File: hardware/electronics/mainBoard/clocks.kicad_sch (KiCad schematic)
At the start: 6 parts, among them X1 ECS-327ATQ2016MV, X2 ECS-2016MVQ, X3 ECS-2016MVQ

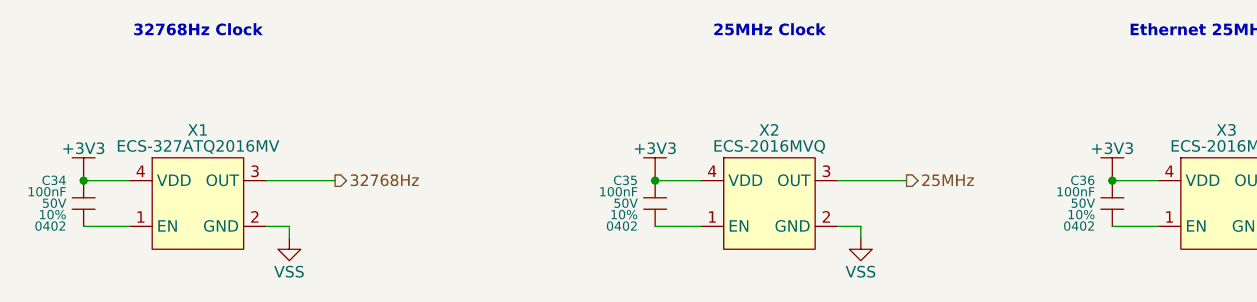
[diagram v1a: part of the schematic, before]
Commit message: updated symbol refs
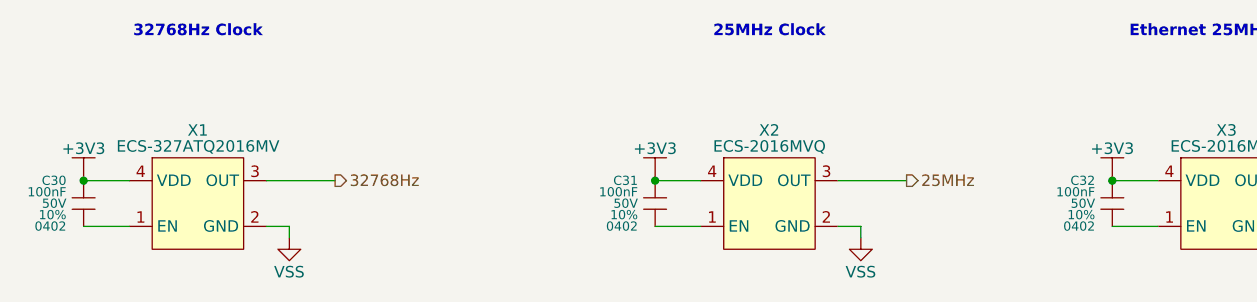
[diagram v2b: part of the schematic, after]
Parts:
- renumbered C34 to C30, C35 to C31, C36 to C32
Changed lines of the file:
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@@
 		(dnp no)
 		(fields_autoplaced yes)
-		(property "Reference" "#PWR082"
+		(property "Reference" "#PWR077"
 			(at 177.8 105.41 0)
 			(effects
@@
 			(project "mainBoard"
 				(path "/be16e32f-2ccf-4272-9ec7-94d5fe7a55e0/7c38f482-70e6-459c-b3af-acf1cdcfd3ea"
-					(reference "#PWR082")
+					(reference "#PWR077")
 					(unit 1)
 				)
@@
 		(dnp no)
 		(fields_autoplaced yes)
-		(property "Reference" "#PWR083"
+		(property "Reference" "#PWR080"
 			(at 200.66 111.76 0)
 			(effects
@@
 			(project "mainBoard"
 				(path "/be16e32f-2ccf-4272-9ec7-94d5fe7a55e0/7c38f482-70e6-459c-b3af-acf1cdcfd3ea"
-					(reference "#PWR083")
+					(reference "#PWR080")
 					(unit 1)
 				)
@@
 		(on_board yes)
 		(dnp no)
-		(property "Reference" "C35"
+		(property "Reference" "C31"
 			(at 125.095 105.41 0)
 			(do_not_autoplace yes)
@@
 			(project "mainBoard"
 				(path "/be16e32f-2ccf-4272-9ec7-94d5fe7a55e0/7c38f482-70e6-459c-b3af-acf1cdcfd3ea"
-					(reference "C35")
+					(reference "C31")
 					(unit 1)
 				)
@@
 		(on_board yes)
 		(dnp no)
-		(property "Reference" "C34"
+		(property "Reference" "C30"
 			(at 61.595 105.41 0)
 			(do_not_autoplace yes)
@@
 			(project "mainBoard"
 				(path "/be16e32f-2ccf-4272-9ec7-94d5fe7a55e0/7c38f482-70e6-459c-b3af-acf1cdcfd3ea"
-					(reference "C34")
+					(reference "C30")
 					(unit 1)
 				)
@@
 		(dnp no)
 		(fields_autoplaced yes)
-		(property "Reference" "#PWR081"
+		(property "Reference" "#PWR079"
 			(at 149.86 111.76 0)
 			(effects
@@
 			(project "mainBoard"
 				(path "/be16e32f-2ccf-4272-9ec7-94d5fe7a55e0/7c38f482-70e6-459c-b3af-acf1cdcfd3ea"
-					(reference "#PWR081")
+					(reference "#PWR079")
 					(unit 1)
 				)
@@
 		(dnp no)
 		(fields_autoplaced yes)
-		(property "Reference" "#PWR078"
+		(property "Reference" "#PWR075"
 			(at 63.5 105.41 0)
 			(effects
@@
 			(project "mainBoard"
 				(path "/be16e32f-2ccf-4272-9ec7-94d5fe7a55e0/7c38f482-70e6-459c-b3af-acf1cdcfd3ea"
-					(reference "#PWR078")
+					(reference "#PWR075")
 					(unit 1)
 				)
@@
 		(on_board yes)
 		(dnp no)
-		(property "Reference" "C36"
+		(property "Reference" "C32"
 			(at 175.895 105.41 0)
 			(do_not_autoplace yes)
@@
 			(project "mainBoard"
 				(path "/be16e32f-2ccf-4272-9ec7-94d5fe7a55e0/7c38f482-70e6-459c-b3af-acf1cdcfd3ea"
-					(reference "C36")
+					(reference "C32")
 					(unit 1)
 				)
@@
 		(dnp no)
 		(fields_autoplaced yes)
-		(property "Reference" "#PWR079"
+		(property "Reference" "#PWR078"
 			(at 86.36 111.76 0)
 			(effects
@@
 			(project "mainBoard"
 				(path "/be16e32f-2ccf-4272-9ec7-94d5fe7a55e0/7c38f482-70e6-459c-b3af-acf1cdcfd3ea"
-					(reference "#PWR079")
+					(reference "#PWR078")
 					(unit 1)
 				)
@@
 		(dnp no)
 		(fields_autoplaced yes)
-		(property "Reference" "#PWR080"
+		(property "Reference" "#PWR076"
 			(at 127 105.41 0)
 			(effects
@@
 			(project "mainBoard"
 				(path "/be16e32f-2ccf-4272-9ec7-94d5fe7a55e0/7c38f482-70e6-459c-b3af-acf1cdcfd3ea"
-					(reference "#PWR080")
-					(unit 1)
-				)
+					(reference "#PWR076")
+					(unit 1)
+				)

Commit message: assigned FPs
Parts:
- X1: footprint (none) -> lib_crystals:ECS-xxxATQ2016MV
- X2, X3: footprint (none) -> lib_crystals:ECS-2016MV
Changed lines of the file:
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@@
 			)
 		)
-		(property "Footprint" ""
+		(property "Footprint" "lib_crystals:ECS-xxxATQ2016MV"
 			(at 76.2 107.95 0)
 			(effects
@@
 			)
 		)
-		(property "Footprint" ""
+		(property "Footprint" "lib_crystals:ECS-2016MV"
 			(at 139.7 107.95 0)
 			(effects
@@
 			)
 		)
-		(property "Footprint" ""
+		(property "Footprint" "lib_crystals:ECS-2016MV"
 			(at 190.5 107.95 0)
 			(effects

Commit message: assigned footprints
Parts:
- C30, C31, C32: footprint (none) -> lib_passives:GCM0402
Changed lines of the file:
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@@
 	(title_block
 		(title "Clocks")
-		(date "2025-03-15")
+		(date "2025-03-20")
 		(rev "1")
 		(comment 2 "PROTOTYPE")
@@
 		(dnp no)
 		(fields_autoplaced yes)
-		(property "Reference" "#PWR077"
+		(property "Reference" "#PWR079"
 			(at 177.8 105.41 0)
 			(effects
@@
 			(project "mainBoard"
 				(path "/be16e32f-2ccf-4272-9ec7-94d5fe7a55e0/7c38f482-70e6-459c-b3af-acf1cdcfd3ea"
-					(reference "#PWR077")
+					(reference "#PWR079")
 					(unit 1)
 				)
@@
 			)
 		)
-		(property "Footprint" ""
+		(property "Footprint" "lib_passives:GCM0402"
 			(at 127 106.045 0)
 			(effects
@@
 			)
 		)
-		(property "Footprint" ""
+		(property "Footprint" "lib_passives:GCM0402"
 			(at 63.5 106.045 0)
 			(effects
@@
 		(dnp no)
 		(fields_autoplaced yes)
-		(property "Reference" "#PWR079"
+		(property "Reference" "#PWR078"
 			(at 149.86 111.76 0)
 			(effects
@@
 			(project "mainBoard"
 				(path "/be16e32f-2ccf-4272-9ec7-94d5fe7a55e0/7c38f482-70e6-459c-b3af-acf1cdcfd3ea"
-					(reference "#PWR079")
+					(reference "#PWR078")
 					(unit 1)
 				)
@@
 			)
 		)
-		(property "Footprint" ""
+		(property "Footprint" "lib_passives:GCM0402"
 			(at 177.8 106.045 0)
 			(effects
@@
 		(dnp no)
 		(fields_autoplaced yes)
-		(property "Reference" "#PWR078"
+		(property "Reference" "#PWR076"
 			(at 86.36 111.76 0)
 			(effects
@@
 			(project "mainBoard"
 				(path "/be16e32f-2ccf-4272-9ec7-94d5fe7a55e0/7c38f482-70e6-459c-b3af-acf1cdcfd3ea"
-					(reference "#PWR078")
+					(reference "#PWR076")
 					(unit 1)
 				)
@@
 		(dnp no)
 		(fields_autoplaced yes)
-		(property "Reference" "#PWR076"
+		(property "Reference" "#PWR077"
 			(at 127 105.41 0)
 			(effects
@@
 			(project "mainBoard"
 				(path "/be16e32f-2ccf-4272-9ec7-94d5fe7a55e0/7c38f482-70e6-459c-b3af-acf1cdcfd3ea"
-					(reference "#PWR076")
+					(reference "#PWR077")
 					(unit 1)
 				)

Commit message: added debugger stuff
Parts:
- added C154, C155: 100nF, lib_passives:GCM0402, symbol lib_sch:C
- added X4: ECS-327ATQ2016MV, lib_crystals:ECS-xxxATQ2016MV, symbol lib_sch:ECS_XTAL_4-SMD
- added X5: ECS-2016MVQ-120, lib_crystals:ECS-2016MV, symbol lib_sch:ECS_XTAL_4-SMD
- X2: value ECS-2016MVQ -> ECS-2016MVQ-250
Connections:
- net VSS: now also X4.2 (GND), X5.2 (GND)
- new net: C155.2, X5.1 (EN)
- new net: C154.2, X4.1 (EN)
- new net +3V3_DBG_H7: C154.1, C155.1, X4.4 (VDD), X5.4 (VDD)
- new net Debug_12MHz: X5.3 (OUT)
- new net Debug_32768Hz: X4.3 (OUT)
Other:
- note added: "12MHz Debugger Clock"
- note added: "32.768kHz Clock"
- note added: "32.768kHz Debugger Clock"
- note removed: "32768Hz Clock"
- moved on the sheet: C30, C31, C32, X1, X2, X3

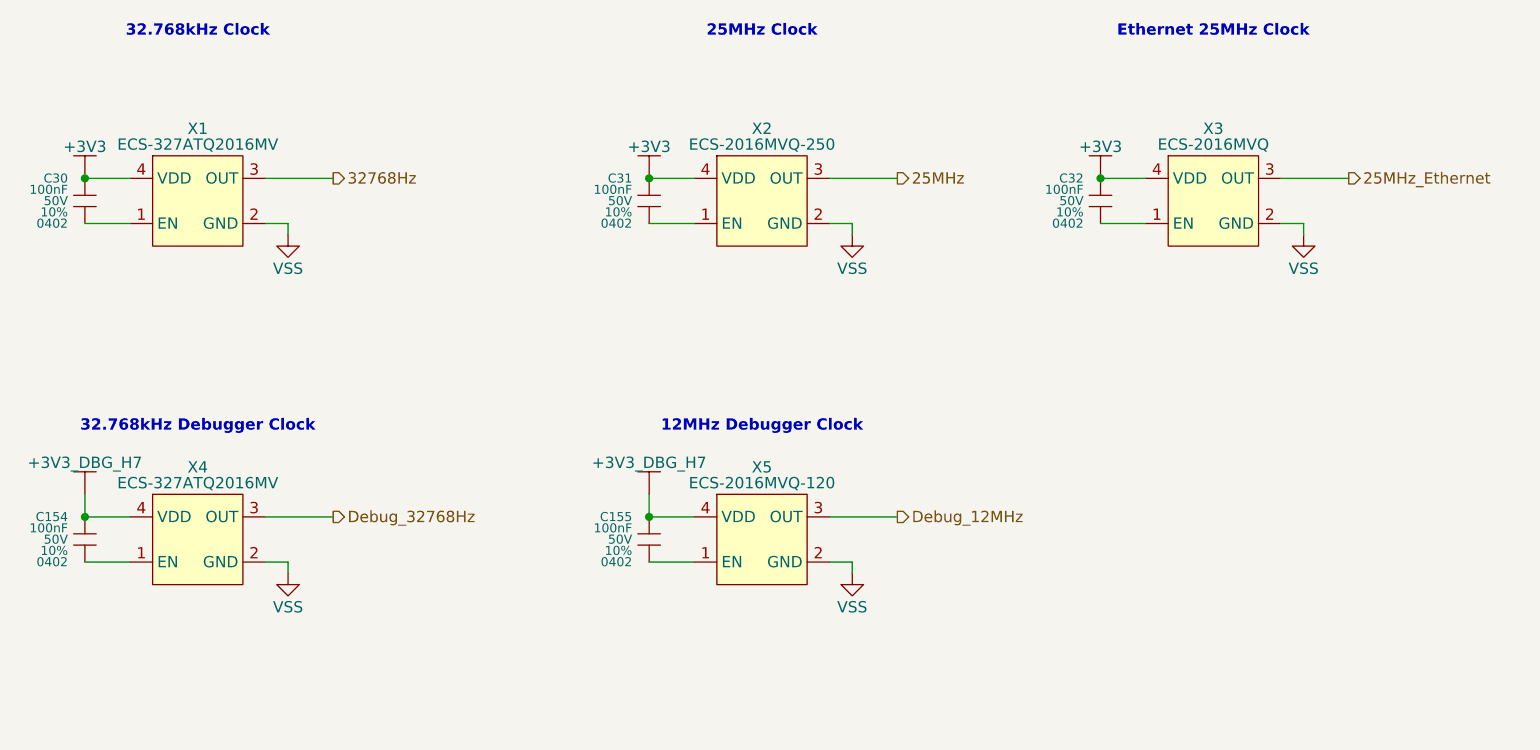
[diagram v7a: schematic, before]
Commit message: removed debugger clocks
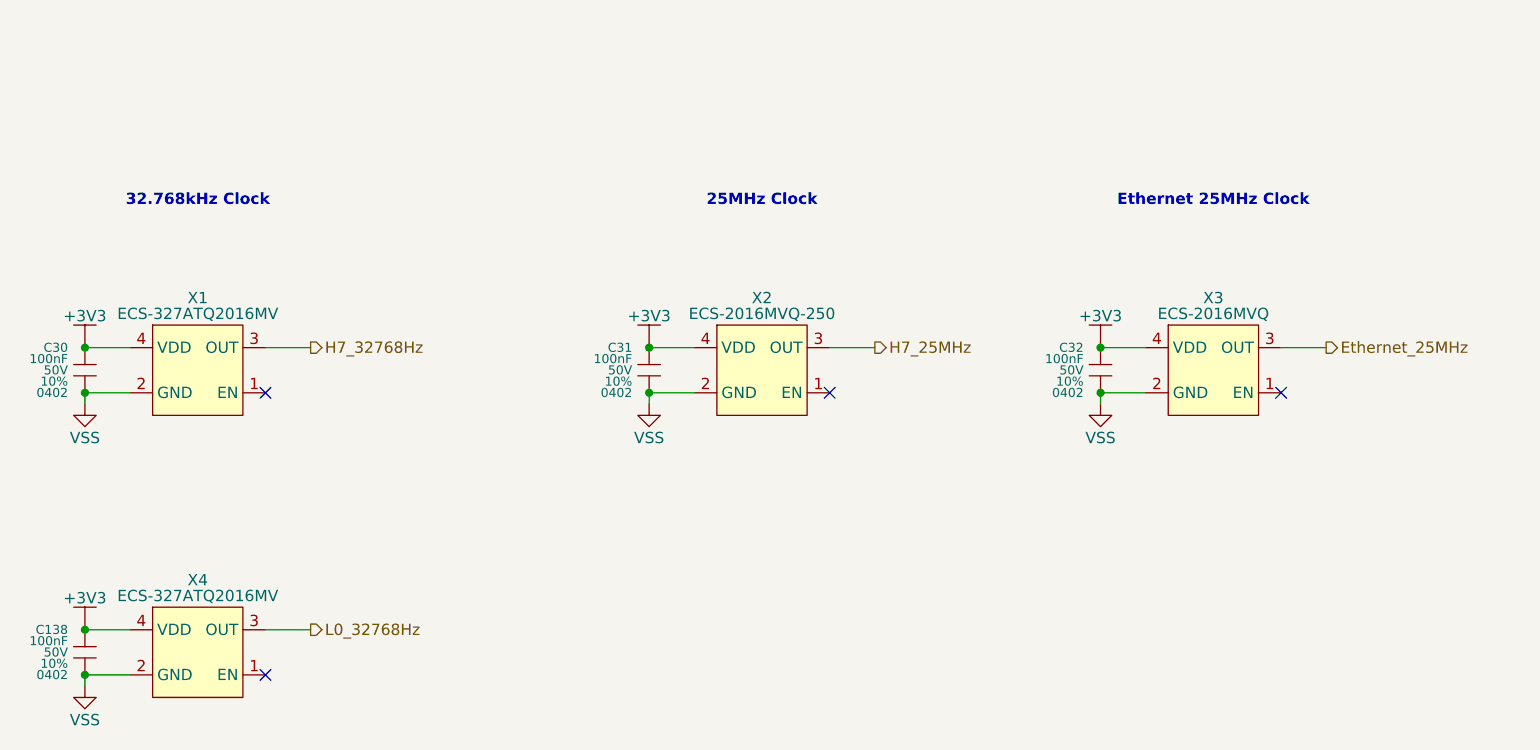
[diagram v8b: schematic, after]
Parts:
- removed C154, C155: 100nF, lib_passives:GCM0402, symbol lib_sch:C
- removed X5: ECS-2016MVQ-120, lib_crystals:ECS-2016MV, symbol lib_sch:ECS_XTAL_4-SMD
- added C138: 100nF, lib_passives:GCM0402, symbol lib_sch:C
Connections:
- net +3V3_DBG_H7 is gone; now on net +3V3: X4.4 (VDD)
- net +3V3: now also C138.1
- net VSS: now also C30.2, C31.2, C32.2, C138.2
- net at X1.1 (EN): no longer C30.2
- net at X2.1 (EN): no longer C31.2
- net at X3.1 (EN): no longer C32.2
- net 25MHz renamed H7_25MHz
- net 25MHz_Ethernet renamed Ethernet_25MHz
- net 32768Hz renamed H7_32768Hz
- net Debug_32768Hz renamed L0_32768Hz
- no-connect marks 0 -> 4
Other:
- note removed: "12MHz Debugger Clock"
- note removed: "32.768kHz Debugger Clock"
- moved on the sheet: C30, C31, C32, X1, X2, X3
